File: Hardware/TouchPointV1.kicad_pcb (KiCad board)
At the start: 2 copper layers, 9.2 x 8.8 mm, 3 parts, among them J1 Conn_01x01_Female, J2 Conn_01x01_Female, SW1 SW_Push_Open

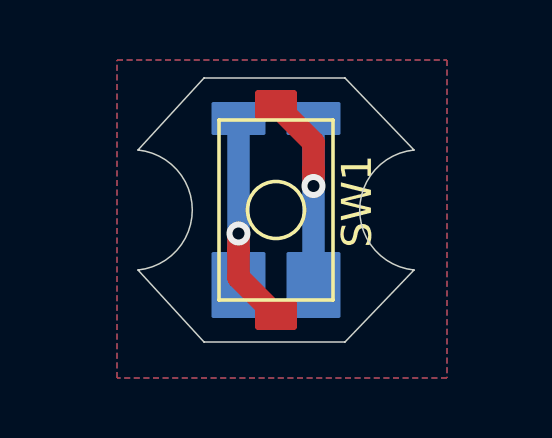
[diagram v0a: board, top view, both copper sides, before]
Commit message: Redesigned board to use M2 holes, exported .STEP and generated iBOM.
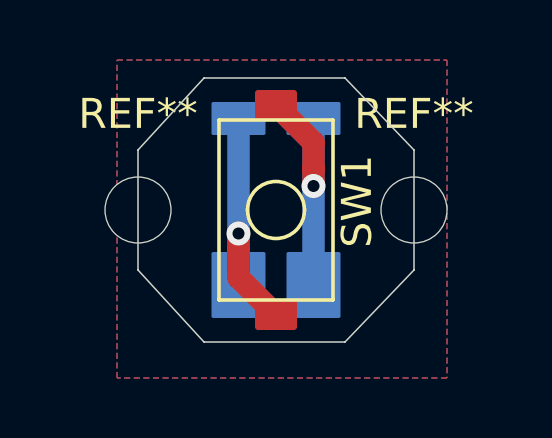
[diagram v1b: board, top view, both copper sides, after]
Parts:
- added REF**: MountingHole_2.2mm_M2, MountingHole:MountingHole_2.2mm_M2, F.Cu at (45.4, 50.0)
- added REF**: MountingHole_2.2mm_M2, MountingHole:MountingHole_2.2mm_M2, F.Cu at (54.6, 50.0)
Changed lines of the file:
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@@
-(kicad_pcb (version 20171130) (host pcbnew "(5.1.4)-1")
+(kicad_pcb (version 20171130) (host pcbnew 5.1.5+dfsg1-2build2)
   (general
     (thickness 1.6)
@@
     (tracks 12)
     (zones 0)
-    (modules 3)
+    (modules 5)
     (nets 3)
   )
@@
     (visible_elements 7FFFEFFF)
     (pcbplotparams
-      (layerselection 0x010fc_ffffffff)
+      (layerselection 0x00000_ffffffff)
       (usegerberextensions false)
       (usegerberattributes false)
       (usegerberadvancedattributes false)
       (creategerberjobfile false)
-      (excludeedgelayer true)
+      (excludeedgelayer false)
       (linewidth 0.100000)
       (plotframeref false)
@@
       (padsonsilk false)
       (subtractmaskfromsilk false)
-      (outputformat 1)
+      (outputformat 4)
       (mirror false)
-      (drillshape 1)
+      (drillshape 2)
       (scaleselection 1)
-      (outputdirectory ""))
+      (outputdirectory "LayerMasks/"))
   )
   (net 0 "")
@@
     (add_net GND)
     (add_net "Net-(J1-Pad1)")
+  )
+  (module MountingHole:MountingHole_2.2mm_M2 (layer F.Cu)
+    (at 45.4 50)
+    (descr "Mounting Hole 2.2mm, no annular, M2")
+    (tags "mounting hole 2.2mm no annular m2")
+    (attr virtual)
+    (fp_text reference REF** (at 0 -3.2) (layer F.SilkS)
+      (effects (font (size 1 1) (thickness 0.15)))
+    )
+    (fp_text value MountingHole_2.2mm_M2 (at 0 3.2) (layer F.Fab)
+      (effects (font (size 1 1) (thickness 0.15)))
+    )
+    (fp_text user %R (at 0.3 0) (layer F.Fab)
+      (effects (font (size 1 1) (thickness 0.15)))
+    )
+    (fp_circle (center 0 0) (end 2.2 0) (layer Cmts.User) (width 0.15))
+    (fp_circle (center 0 0) (end 2.45 0) (layer F.CrtYd) (width 0.05))
+    (pad 1 np_thru_hole circle (at 0 0) (size 2.2 2.2) (drill 2.2) (layers *.Cu *.Mask))
+  )
+  (module MountingHole:MountingHole_2.2mm_M2 (layer F.Cu)
+    (at 54.6 50)
+    (descr "Mounting Hole 2.2mm, no annular, M2")
+    (tags "mounting hole 2.2mm no annular m2")
+    (attr virtual)
+    (fp_text reference REF** (at 0 -3.2) (layer F.SilkS)
+      (effects (font (size 1 1) (thickness 0.15)))
+    )
+    (fp_text value MountingHole_2.2mm_M2 (at 0 3.2) (layer F.Fab)
+      (effects (font (size 1 1) (thickness 0.15)))
+    )
+    (fp_circle (center 0 0) (end 2.45 0) (layer F.CrtYd) (width 0.05))
+    (fp_circle (center 0 0) (end 2.2 0) (layer Cmts.User) (width 0.15))
+    (fp_text user %R (at 0.3 0) (layer F.Fab)
+      (effects (font (size 1 1) (thickness 0.15)))
+    )
+    (pad 1 np_thru_hole circle (at 0 0) (size 2.2 2.2) (drill 2.2) (layers *.Cu *.Mask))
   )
   (module TouchPointV1:AVX-709296001017006 (layer B.Cu)
@@
     )
   )
+  (gr_line (start 54.600001 48.000001) (end 54.600739 52.000073) (layer Edge.Cuts) (width 0.05))
+  (gr_line (start 45.400001 48.000001) (end 45.399999 51.999999) (layer Edge.Cuts) (width 0.05))
   (gr_line (start 52.3 45.6) (end 54.600001 48.000001) (layer Edge.Cuts) (width 0.05))
   (gr_line (start 45.400001 48.000001) (end 47.6 45.6) (layer Edge.Cuts) (width 0.05))
@@
   (gr_line (start 52.3 54.4) (end 47.6 54.4) (layer Edge.Cuts) (width 0.05))
   (gr_line (start 52.3 45.6) (end 47.6 45.6) (layer Edge.Cuts) (width 0.05))
-  (gr_arc (start 45.2 50) (end 45.399999 51.999999) (angle -168.5788137) (layer Edge.Cuts) (width 0.05))
-  (gr_arc (start 54.8 50) (end 54.600001 48.000001) (angle -168.6) (layer Edge.Cuts) (width 0.05))
   (via (at 48.75 50.78318) (size 0.8) (drill 0.4) (layers F.Cu B.Cu) (net 1))
   (segment (start 48.75 52.5) (end 48.75 50.78318) (width 0.75) (layer B.Cu) (net 1))
